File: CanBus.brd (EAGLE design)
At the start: 80 x 100 mm, 47 parts, among them IC1 MCP2515-I/SO, IC2 MEGA8-P, IC3 MCP2515-I/SO, Q1 16MHz, Q2 16MHz, Q3 16MHz, U1 MCP2562-E/SN, U2 MCP2562-E/SN, X1 MAC64L

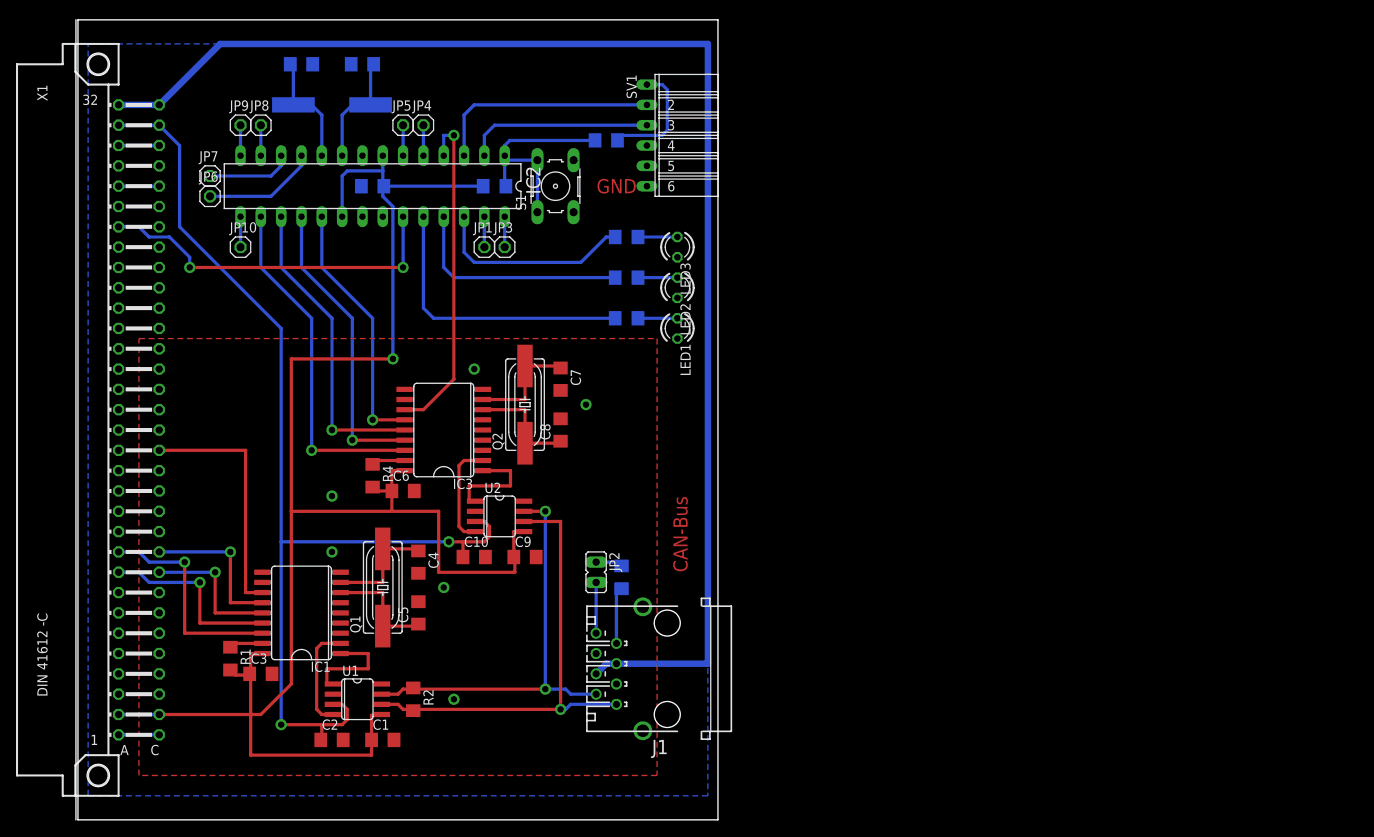
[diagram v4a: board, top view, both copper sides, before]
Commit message: Pi-Display hinzugefügt, Boards angepasst
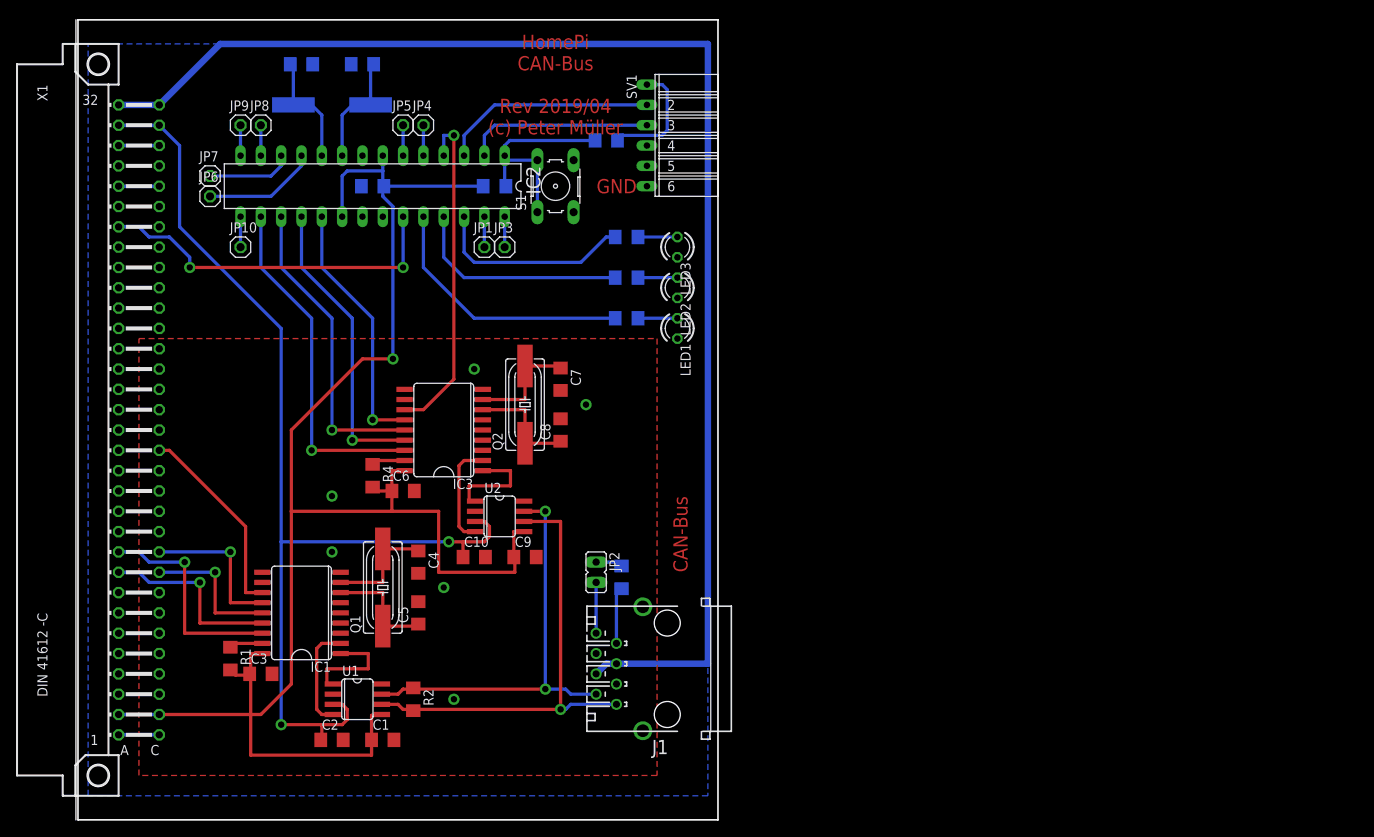
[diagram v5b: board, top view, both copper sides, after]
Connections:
- removed net N$12: C13.1, C14.1
- net GND: now also C13.1, C14.1
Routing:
- net GPIO.06: track 30.7 -> 25.1 mm
- net +3,3V: track 215.2 -> 210.3 mm
- net LED1: track 35.9 -> 33.0 mm
- net PROG_RX: track 28.5 -> 27.0 mm
- net +5V_EXT: track 130.5 -> 131.7 mm
- net LED2: track 28.3 -> 27.6 mm
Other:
- board text added: "HomePi CAN-Bus Rev 2019/04 (c) Peter Müller"
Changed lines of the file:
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@@
 <board>
 <plain>
-<wire x1="0" y1="-0.47" x2="80" y2="-0.47" width="0" layer="20"/>
-<wire x1="80" y1="-0.47" x2="80" y2="99.53" width="0" layer="20"/>
-<wire x1="80" y1="99.53" x2="0" y2="99.53" width="0" layer="20"/>
-<wire x1="0" y1="99.53" x2="0" y2="-0.47" width="0" layer="20"/>
+<wire x1="0" y1="-0.47" x2="80" y2="-0.47" width="0.2" layer="20"/>
+<wire x1="80" y1="-0.47" x2="80" y2="99.53" width="0.2" layer="20"/>
+<wire x1="80" y1="99.53" x2="0" y2="99.53" width="0.2" layer="20"/>
+<wire x1="0" y1="99.53" x2="0" y2="-0.47" width="0.2" layer="20"/>
 <text x="76.2" y="30.48" size="1.778" layer="1" font="vector" ratio="15" rot="R90">CAN-Bus</text>
 <rectangle x1="41.91" y1="51.054" x2="42.672" y2="53.848" layer="41"/>
@@
 <rectangle x1="48.768" y1="42.672" x2="49.53" y2="44.196" layer="41"/>
 <rectangle x1="48.768" y1="44.704" x2="49.53" y2="53.086" layer="41"/>
-<rectangle x1="50.8" y1="37.084" x2="51.308" y2="39.878" layer="41"/>
 <rectangle x1="24.13" y1="19.812" x2="24.892" y2="30.988" layer="41"/>
 <rectangle x1="30.988" y1="21.844" x2="31.75" y2="30.226" layer="41"/>
@@
 <rectangle x1="54.102" y1="35.814" x2="54.61" y2="39.116" layer="41"/>
 <text x="69.85" y="78.74" size="1.778" layer="1" font="vector" ratio="15" align="center-right">GND</text>
+<dimension x1="0" y1="-0.47" x2="0" y2="99.53" x3="-16.51" y3="49.53" textsize="1.778" layer="20" visible="yes"/>
+<dimension x1="0" y1="-0.47" x2="80" y2="-0.47" x3="40" y3="-8.89" textsize="1.778" layer="20" visible="yes"/>
+<rectangle x1="50.8" y1="38.608" x2="51.308" y2="39.878" layer="41"/>
+<rectangle x1="50.8" y1="37.084" x2="51.308" y2="37.592" layer="41"/>
+<text x="59.69" y="91.44" size="1.778" layer="1" ratio="15" rot="R180" align="center">HomePi
+CAN-Bus
+Rev 2019/04
+(c) Peter Müller</text>
 </plain>
 <attributes>
@@
 <contactref element="X1" pad="C15"/>
 <wire x1="23.0378" y1="27.94" x2="20.955" y2="27.94" width="0.4064" layer="1"/>
-<wire x1="20.955" y1="27.94" x2="20.955" y2="45.72" width="0.4064" layer="1"/>
-<wire x1="20.955" y1="45.72" x2="10.16" y2="45.72" width="0.4064" layer="1"/>
+<wire x1="20.955" y1="27.94" x2="20.955" y2="36.195" width="0.4064" layer="1"/>
+<wire x1="20.955" y1="36.195" x2="11.43" y2="45.72" width="0.4064" layer="1"/>
+<wire x1="11.43" y1="45.72" x2="10.16" y2="45.72" width="0.4064" layer="1"/>
 </signal>
 <signal name="GPIO.12">
@@
 <wire x1="38.1" y1="80.645" x2="38.1" y2="78.87" width="0.4064" layer="16"/>
 <wire x1="26.67" y1="16.51" x2="26.67" y2="38.1" width="0.4064" layer="1"/>
-<wire x1="26.67" y1="38.1" x2="26.67" y2="57.15" width="0.4064" layer="1"/>
 <wire x1="39.24" y1="38.1" x2="26.67" y2="38.1" width="0.4064" layer="1"/>
-<wire x1="26.67" y1="57.15" x2="39.37" y2="57.15" width="0.4064" layer="1"/>
-<via x="39.37" y="57.15" extent="1-16" drill="0.8" diameter="1.4224"/>
-<wire x1="39.37" y1="57.15" x2="39.37" y2="76.2" width="0.4064" layer="16"/>
 <wire x1="39.37" y1="76.2" x2="38.1" y2="77.47" width="0.4064" layer="16"/>
 <wire x1="38.1" y1="77.47" x2="38.1" y2="78.61" width="0.4064" layer="16"/>
 <wire x1="38.1" y1="78.61" x2="38.23" y2="78.74" width="0.4064" layer="16"/>
 <wire x1="50.648" y1="78.74" x2="38.23" y2="78.74" width="0.4064" layer="16"/>
-<wire x1="38.23" y1="78.74" x2="38.1" y2="78.87" width="0" layer="19" extent="16-16"/>
-<wire x1="21.46" y1="17.78" x2="21.438" y2="17.628" width="0" layer="19" extent="1-1"/>
+<wire x1="21.46" y1="17.78" x2="21.438" y2="17.758" width="0.4064" layer="1"/>
+<wire x1="21.438" y1="17.758" x2="21.438" y2="17.628" width="0.4064" layer="1"/>
+<wire x1="38.23" y1="78.74" x2="38.1" y2="78.87" width="0.4064" layer="16"/>
+<wire x1="26.67" y1="38.1" x2="26.67" y2="48.26" width="0.4064" layer="1"/>
+<wire x1="39.37" y1="76.2" x2="39.37" y2="57.15" width="0.4064" layer="16"/>
+<via x="39.37" y="57.15" extent="1-16" drill="0.8" diameter="1.4224"/>
+<wire x1="39.37" y1="57.15" x2="35.56" y2="57.15" width="0.4064" layer="1"/>
+<wire x1="35.56" y1="57.15" x2="26.67" y2="48.26" width="0.4064" layer="1"/>
 </signal>
 <signal name="+5V_INT2">
@@
 <wire x1="12.7" y1="73.66" x2="12.7" y2="83.82" width="0.4064" layer="16"/>
 <wire x1="12.7" y1="83.82" x2="10.16" y2="86.36" width="0.4064" layer="16"/>
-<wire x1="33.02" y1="13.97" x2="31.8516" y2="13.97" width="0" layer="19" extent="1-1"/>
+<wire x1="31.8516" y1="13.97" x2="33.02" y2="13.97" width="0.4064" layer="1"/>
 </signal>
 <signal name="+24V">
@@
 <via x="49.53" y="55.88" extent="1-16" drill="0.8" diameter="1.4224"/>
 <via x="31.75" y="33.02" extent="1-16" drill="0.8" diameter="1.4224"/>
-<wire x1="49.6316" y1="38.1" x2="50.93" y2="32.385" width="0" layer="19" extent="1-1"/>
+<contactref element="C13" pad="1"/>
+<contactref element="C14" pad="1"/>
 </signal>
 <signal name="TXCAN">
@@
 <contactref element="SV1" pad="2"/>
 <contactref element="IC2" pad="3"/>
-<wire x1="71.12" y1="88.9" x2="49.53" y2="88.9" width="0.4064" layer="16"/>
-<wire x1="49.53" y1="88.9" x2="48.26" y2="87.63" width="0.4064" layer="16"/>
-<wire x1="48.26" y1="87.63" x2="48.26" y2="82.55" width="0.4064" layer="16"/>
+<wire x1="71.12" y1="88.9" x2="52.07" y2="88.9" width="0.4064" layer="16"/>
+<wire x1="52.07" y1="88.9" x2="48.26" y2="85.09" width="0.4064" layer="16"/>
+<wire x1="48.26" y1="85.09" x2="48.26" y2="82.55" width="0.4064" layer="16"/>
 </signal>
 <signal name="PROG_TX">
@@
 <wire x1="26.924" y1="93.596" x2="26.54" y2="93.98" width="0.4064" layer="16"/>
 </signal>
-<signal name="N$12">
-<contactref element="C13" pad="1"/>
-<contactref element="C14" pad="1"/>
-<wire x1="29.34" y1="93.98" x2="34.16" y2="93.98" width="0" layer="19" extent="16-16"/>
-</signal>
 <signal name="AT_INT0">
 <contactref element="IC3" pad="12"/>
@@
 <contactref element="R6" pad="2"/>
 <contactref element="IC2" pad="24"/>
-<wire x1="67.158" y1="62.23" x2="44.45" y2="62.23" width="0.4064" layer="16"/>
-<wire x1="44.45" y1="62.23" x2="43.18" y2="63.5" width="0.4064" layer="16"/>
-<wire x1="43.18" y1="63.5" x2="43.18" y2="74.93" width="0.4064" layer="16"/>
+<wire x1="67.158" y1="62.23" x2="49.53" y2="62.23" width="0.4064" layer="16"/>
+<wire x1="49.53" y1="62.23" x2="43.18" y2="68.58" width="0.4064" layer="16"/>
+<wire x1="43.18" y1="68.58" x2="43.18" y2="74.93" width="0.4064" layer="16"/>
 </signal>
 <signal name="LED3">
@@
 <contactref element="R7" pad="2"/>
 <contactref element="IC2" pad="25"/>
-<wire x1="67.158" y1="67.31" x2="46.99" y2="67.31" width="0.4064" layer="16"/>
-<wire x1="46.99" y1="67.31" x2="45.72" y2="68.58" width="0.4064" layer="16"/>
-<wire x1="45.72" y1="68.58" x2="45.72" y2="74.93" width="0.4064" layer="16"/>
+<wire x1="67.158" y1="67.31" x2="48.26" y2="67.31" width="0.4064" layer="16"/>
+<wire x1="48.26" y1="67.31" x2="45.72" y2="69.85" width="0.4064" layer="16"/>
+<wire x1="45.72" y1="69.85" x2="45.72" y2="74.93" width="0.4064" layer="16"/>
 </signal>
 <signal name="AT_PD5">
@@
 </board>
 </drawing>
+<compatibility>
+<note version="6.3" minversion="6.2.2" severity="warning">
+Since Version 6.2.2 text objects can contain more than one line,
+which will not be processed correctly with this version.
+</note>
+</compatibility>
 </eagle>

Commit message: Layouts aktualisiert, Neue Libs
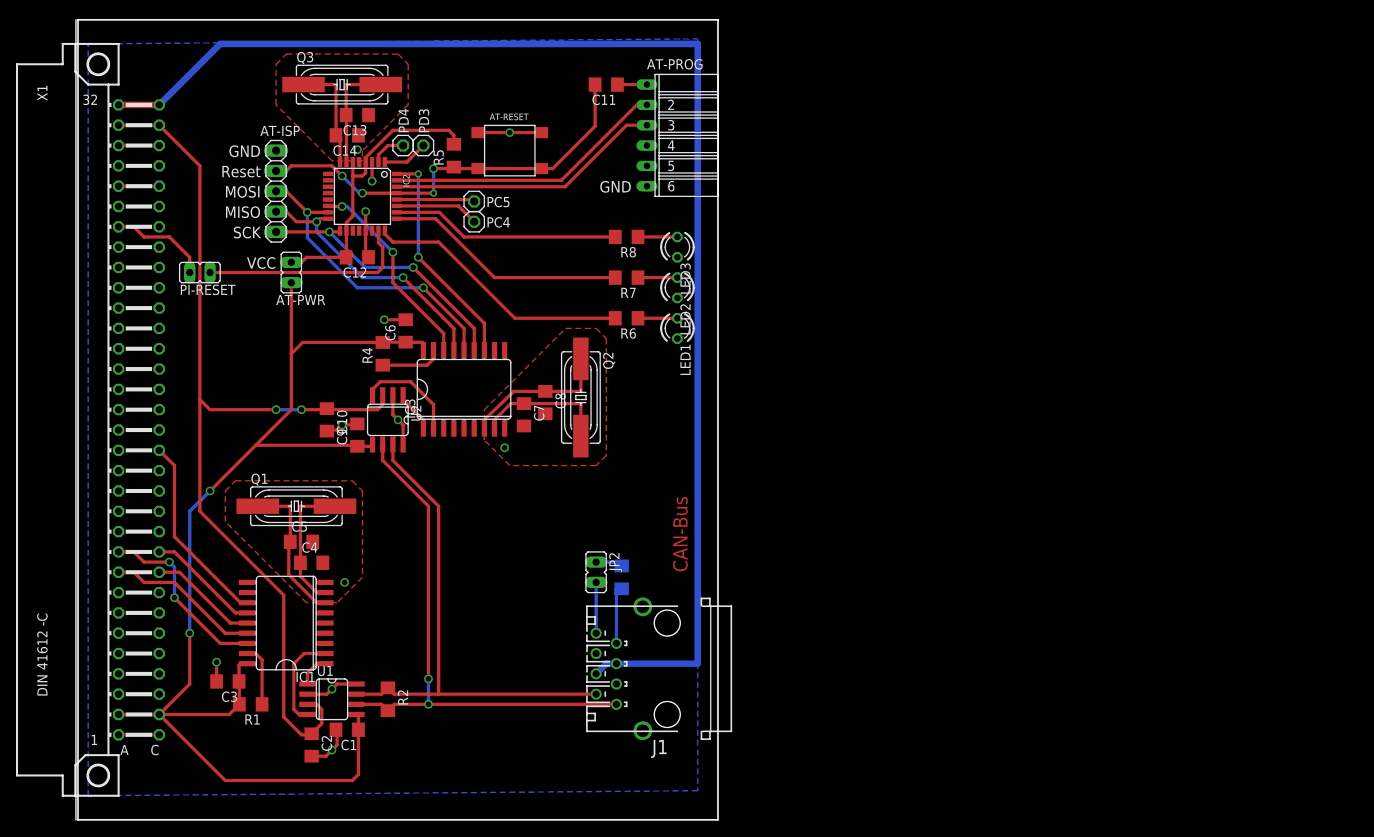
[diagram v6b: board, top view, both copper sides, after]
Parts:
- removed JP1, JP10, JP3, JP4, JP5, JP6, JP7, JP8, JP9: (no value), pinhead:1X01
- removed S1: (no value), switch-omron:B3F-10XX
- added AT-ISP: (no value), pinhead:1X05
- added AT-PWR, PI-RESET: (no value), jumper:JP1
- added AT-RESET: B3FS-1000, b3fs-1000:B3FS-1000
- added PC4, PC5, PD3, PD4: (no value), pinhead:1X01
- IC2: value MEGA8-P -> MEGA8-AI; device atmel:DIL28-3 -> atmel:TQFP32-08
- moved C9 25.9 mm to (34.9, 47.6), turned to 90 degrees
- moved C10 25.2 mm to (31.1, 49.5), turned to 270 degrees
- moved C6 20.0 mm to (41.0, 60.6), turned to 90 degrees
- moved U2 18.5 mm to (38.7, 49.5), turned to 180 degrees
- moved C5 17.1 mm to (27.9, 34.3), turned to 0 degrees
- moved R4 15.3 mm to (38.1, 57.8), turned to 90 degrees
- moved Q1 14.8 mm to (27.3, 38.7), turned to 0 degrees
- moved C4 13.3 mm to (29.2, 31.7), turned to 0 degrees
- moved C14 10.6 mm to (33.7, 85.1), flipped to the top, turned to 180 degrees
- moved C12 9.09 mm to (34.9, 69.8), flipped to the top
- moved Q2 7.04 mm to (62.9, 52.3), turned to 270 degrees
- moved C11 6.98 mm to (66.0, 91.4), flipped to the top, turned to 180 degrees
- moved C13 6.38 mm to (34.9, 87.6), flipped to the top
- moved C7 6.38 mm to (55.8, 50.2)
- moved R5 6.35 mm to (47.0, 82.5), flipped to the top, turned to 90 degrees
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- renumbered SV1 to AT-PROG
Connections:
- removed net N$8: C11.2, IC2.1, R5.1, S1.1, S1.2
- new net !AT_RESET: AT-ISP.4, AT-RESET.3, AT-RESET.4, C11.2, IC2.29, R5.1
- new net AT_VCC: AT-PWR.2, C12.2, IC2.18, IC2.4, IC2.6, R5.2
- new net N$9: IC2.23, PI-RESET.1
- net !PI_RESET: now also PI-RESET.2; no longer IC2.23
- net +3,3V: now also AT-PWR.1; no longer C12.2, IC2.20, IC2.7, R5.2
- net AT_INT0: now also IC2.32; no longer IC2.4
- net AT_PB0: now also IC2.12; no longer IC2.14, JP9.1
- net AT_PB1: now also IC2.13; no longer IC2.15, JP10.1
- net AT_PC4: now also PC4.1; no longer JP1.1
- net AT_PC5: now also PC5.1; no longer JP3.1
- net AT_PD3: now also IC2.1, PD3.1; no longer IC2.5, JP4.1
- net AT_PD4: now also IC2.2, PD4.1; no longer IC2.6, JP5.1
- net AT_PD5: now also IC2.9; no longer IC2.11, JP6.1
- net AT_PD6: now also IC2.10; no longer IC2.12, JP7.1
- net AT_PD7: now also IC2.11; no longer IC2.13, JP8.1
- net AT_SPI_CS: now also IC2.14; no longer IC2.16
- net AT_SPI_MISO: now also AT-ISP.2, IC2.16; no longer IC2.18
- net AT_SPI_MOSI: now also AT-ISP.3, IC2.15; no longer IC2.17
- net AT_SPI_SCK: now also AT-ISP.1, IC2.17; no longer IC2.19
- net GND: now also AT-RESET.1, AT-RESET.2, IC2.21, IC2.3, IC2.5; no longer IC2.22, IC2.8, S1.3, S1.4
- net N$10: now also IC2.7; no longer IC2.9
- net N$11: now also IC2.8; no longer IC2.10
- net PROG_RX: now also IC2.31; no longer IC2.3
- net PROG_TX: now also IC2.30; no longer IC2.2
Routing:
- net +3,3V: track 210.3 -> 151.1 mm, vias 1 -> 2
- net !AT_RESET: track 0.00 -> 52.2 mm, vias 0 -> 4
- net GND: track 0.00 -> 44.6 mm, vias 6 -> 12
- net AT_VCC: track 0.00 -> 36.9 mm
- net !PI_RESET: track 44.8 -> 12.4 mm, vias 2 -> 0
- net N$8: track 27.8 -> 0.00 mm
- net N$9: track 0.00 -> 26.7 mm
- net AT_SPI_CS: track 43.4 -> 25.4 mm, vias 1 -> 2
- net AT_PD5: track 14.3 -> 0.00 mm
- net AT_INT0: track 42.0 -> 28.1 mm, vias 1 -> 2
- net CANH: track 52.4 -> 64.2 mm, vias 2 -> 0
- net +5V_EXT: track 131.7 -> 120.5 mm
- net PROG_TX: track 23.4 -> 34.5 mm
- net PROG_DTR: track 14.6 -> 3.68 mm
- net AT_PD6: track 10.7 -> 0.00 mm
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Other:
- board text added: "MISO"
- board text added: "MOSI"
- board text added: "Reset"
- board text added: "SCK"
- board text added: "VCC"
- board text removed: "HomePi CAN-Bus Rev 2019/04 (c) Peter Müller"

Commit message: Layouts angepasst
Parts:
- added A14, A15, A16, A17, A18, A19, A20, A21, A22, PB0, PB1, PD5, PD6, PD7: (no value), pinhead:1X01
- moved R5 28.8 mm to (18.4, 79.4), turned to 270 degrees
- moved C11 13.9 mm to (56.8, 81.0)
- moved JP2 13.2 mm to (54.0, 22.9), turned to 0 degrees
- moved R3 12.1 mm to (59.1, 21.6), flipped to the top, turned to 180 degrees
- moved PD4 11.1 mm to (46.4, 93.3)
- moved R6 10.2 mm to (59.7, 67.3)
- moved R7 9.25 mm to (59.7, 69.8)
- moved R8 8.89 mm to (59.7, 72.4)
- moved PD3 7.67 mm to (46.4, 90.8)
- moved AT-RESET 5.72 mm to (48.3, 83.2)
- moved AT-PWR 5.12 mm to (21.6, 67.3)
- moved AT-ISP 3.70 mm to (21.6, 76.2)
- moved PI-RESET 0.90 mm to (15.9, 67.3)
- moved C12 0.63 mm to (34.3, 69.8)
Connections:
- new net A14: A14.1, X1.A14
- new net A15: A15.1, X1.A15
- new net A16: A16.1, X1.A16
- new net A17: A17.1, X1.A17
- new net A18: A18.1, X1.A18
- new net A19: A19.1, X1.A19
- new net A20: A20.1, X1.A20
- new net A21: A21.1, X1.A21
- new net A22: A22.1, X1.A22
- new net A23: X1.A23
- new net A24: X1.A24
- new net A25: X1.A25
- new net N$12: X1.A4
- new net N$16: X1.A7
- new net N$8: X1.A5
- net !AT_RESET: now also AT-ISP.5; no longer AT-ISP.4
- net 1WIRE: now also X1.C7; no longer X1.A7
- net AT_PB0: now also PB0.1
- net AT_PB1: now also PB1.1
- net AT_PD5: now also PD5.1
- net AT_PD6: now also PD6.1
- net AT_PD7: now also PD7.1
- net AT_SPI_MISO: now also AT-ISP.3; no longer AT-ISP.2
- net AT_SPI_MOSI: now also AT-ISP.4; no longer AT-ISP.3
- net AT_SPI_SCK: now also AT-ISP.2; no longer AT-ISP.1
- net GND: now also AT-ISP.1, X1.A11, X1.A13, X1.A27, X1.C13
- net I2C_SCL: now also X1.C5; no longer X1.A5
- net I2C_SDA: now also X1.C4; no longer X1.A4
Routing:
- net AT_PB0: track 0.00 -> 21.0 mm
- net AT_PB1: track 0.00 -> 19.7 mm
- net AT_PD5: track 0.00 -> 17.7 mm
- net AT_PD6: track 0.00 -> 16.6 mm
- net AT_PD7: track 0.00 -> 15.9 mm
- net PROG_DTR: track 3.68 -> 17.2 mm
- net LED1: track 33.6 -> 22.6 mm
- net N$14: track 4.93 -> 15.9 mm
- net AT_PD4: track 4.45 -> 15.2 mm
- net LED2: track 30.4 -> 20.4 mm
- net N$15: track 4.93 -> 14.9 mm
- net LED3: track 28.6 -> 19.7 mm
- net N$19: track 4.93 -> 13.8 mm
- net !AT_RESET: track 52.2 -> 43.5 mm, vias 4 -> 1
- net A22: track 0.00 -> 8.15 mm
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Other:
- board text added: "AT-Power"
- board text added: "CAN-2 Terminierung"
- board text added: "DTR"
- board text added: "HomePi CAN-Bus Rev 2019/04 (c) Peter Müller"
- board text added: "Pi-Reset aktiv"
- board text added: "RX"
- board text added: "TX"
